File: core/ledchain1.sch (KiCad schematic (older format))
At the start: 60 parts

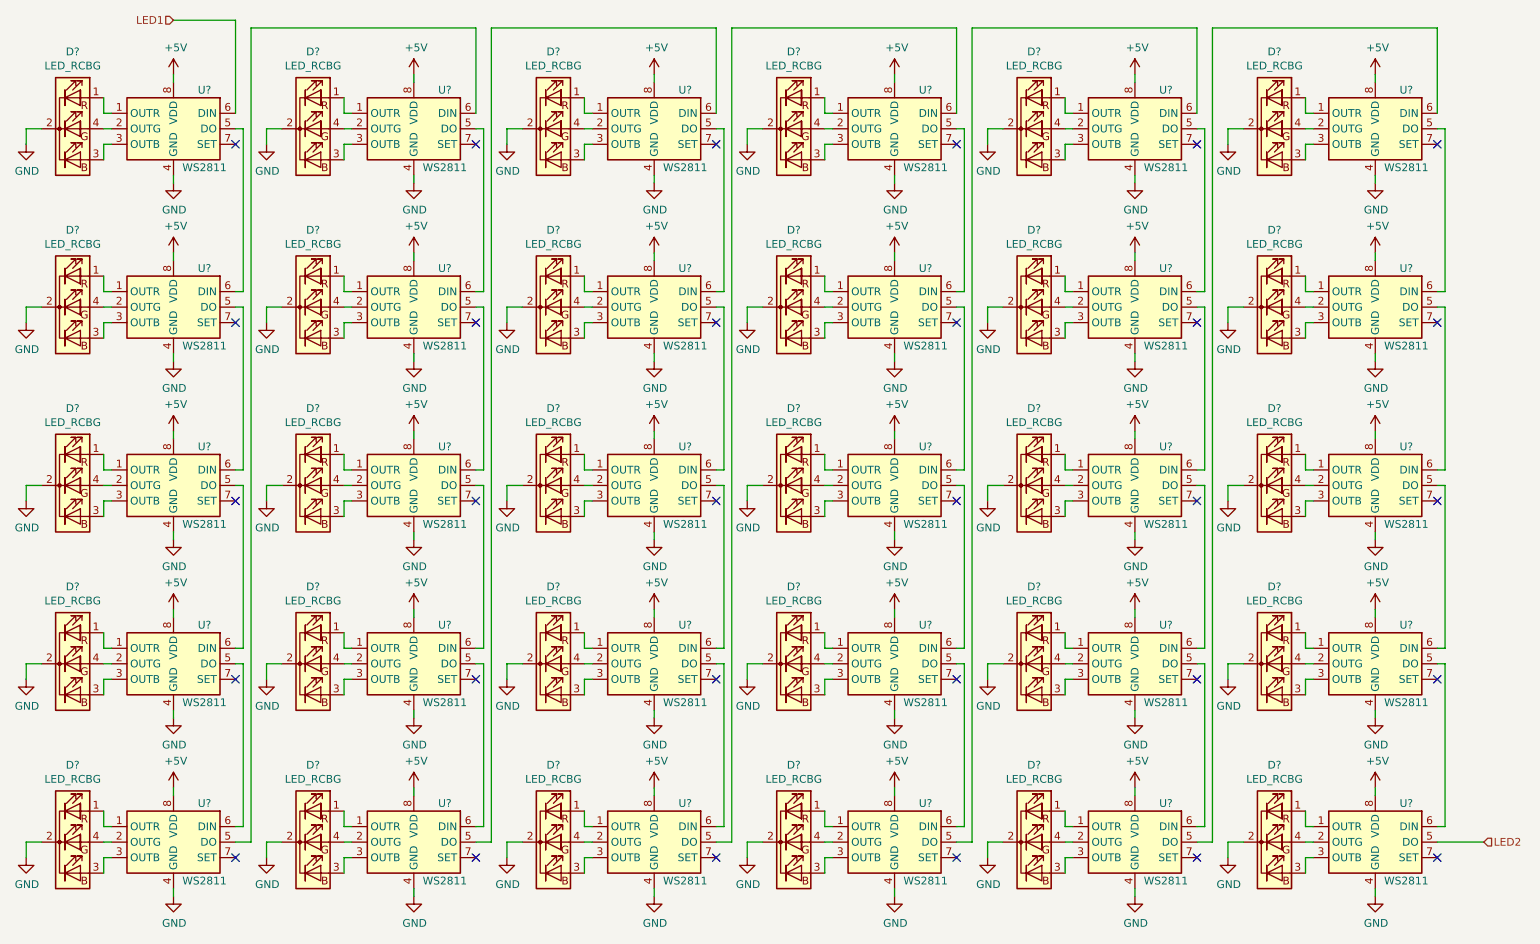
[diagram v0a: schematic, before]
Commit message: annotate led chain
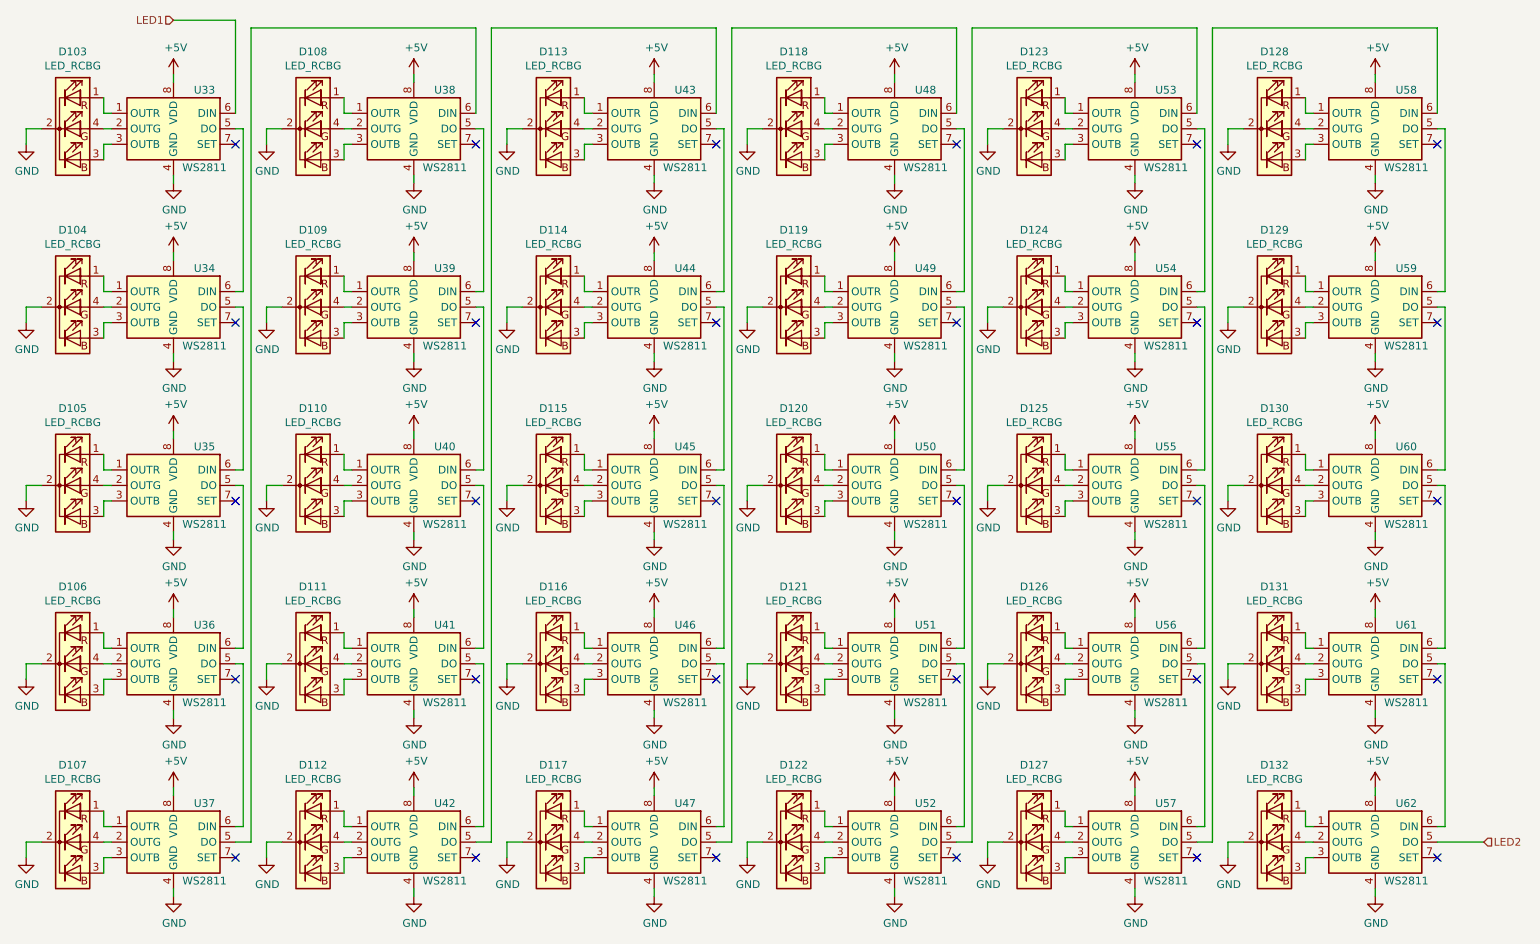
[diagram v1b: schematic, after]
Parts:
- gave numbers to parts that had none: 60
